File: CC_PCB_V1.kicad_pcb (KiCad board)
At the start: 2 copper layers, 104.2 x 144.9 mm, 8 parts, among them J1 Screw_Terminal_01x07, J2 Antenna_Conn_02x04_Odd_Even, J5 Relay_Conn_01x06, U1 Pico, U2 LM337_TO3

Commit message: Pushing so I can edit on my PC
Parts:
- added J3: USB1130-15-A_REVA, MCU_RaspberryPi_and_Boards:GCT_USB1130-15-A_REVA, F.Cu at (87.0, 150.0)
- moved Screw_Terminal1 120.7 mm to (68.0, 155.0), turned to 180 degrees
- moved U2 116.8 mm to (116.0, 152.0)
- moved C1 113.0 mm to (117.0, 137.0)
- moved C2 106.0 mm to (103.5, 140.0)
- moved J2 35.7 mm to (99.0, 116.0), turned to 180 degrees
- moved J5 26.8 mm to (104.0, 40.0)
- moved U1 8.70 mm to (137.0, 59.5)
- moved J1 2.26 mm to (151.0, 97.0), turned to 270 degrees
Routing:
- net +3.3V: track 167.0 -> 0.00 mm
- net GP6: track 86.0 -> 0.00 mm, vias 2 -> 0
- net GP4: track 78.1 -> 0.00 mm, vias 1 -> 0
- net +5V: track 75.7 -> 0.00 mm
- net GP7: track 74.3 -> 0.00 mm, vias 1 -> 0
- net 3.3V: track 68.5 -> 0.00 mm
- net GP17: track 48.9 -> 0.00 mm
- net GP12: track 45.2 -> 0.00 mm, vias 1 -> 0
- net GP27: track 43.9 -> 0.00 mm
- net GP14: track 43.6 -> 0.00 mm
- net GP22: track 40.5 -> 0.00 mm
- net GP26: track 40.4 -> 0.00 mm
- net GP13: track 40.2 -> 0.00 mm
- net GP21: track 36.8 -> 0.00 mm, vias 1 -> 0
- net GND: track 29.2 -> 0.00 mm, vias 5 -> 0
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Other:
- board text added: "+3.3V"
- board text added: "DIR"
- board text added: "On/Off"
- board text added: "POT1"
- board text added: "POT2"
- board text added: "Step"
- board text added: "Throttle"

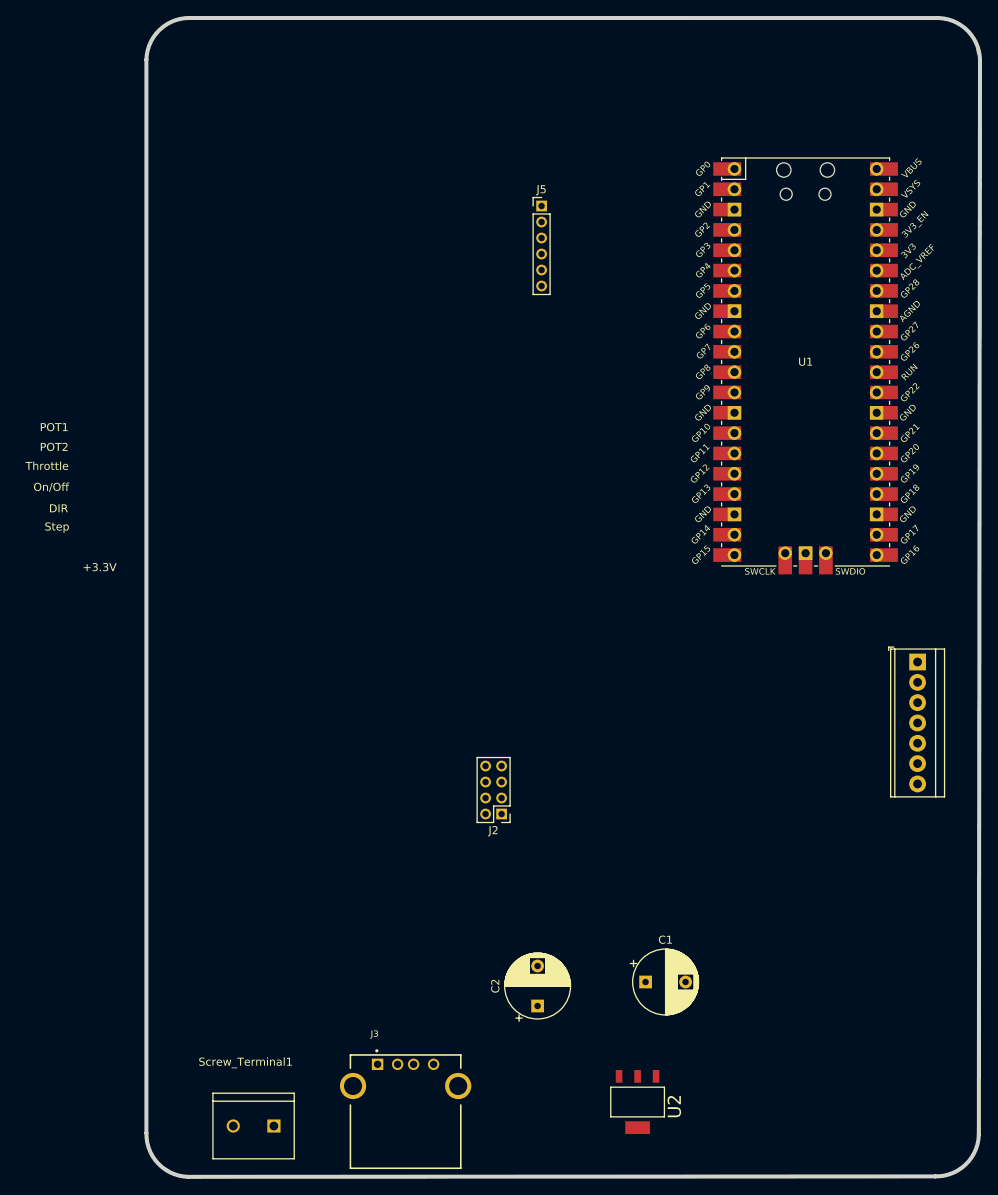
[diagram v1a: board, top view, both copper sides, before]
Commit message: "Finished" PCB
Re did the layout of the board for a better fitment
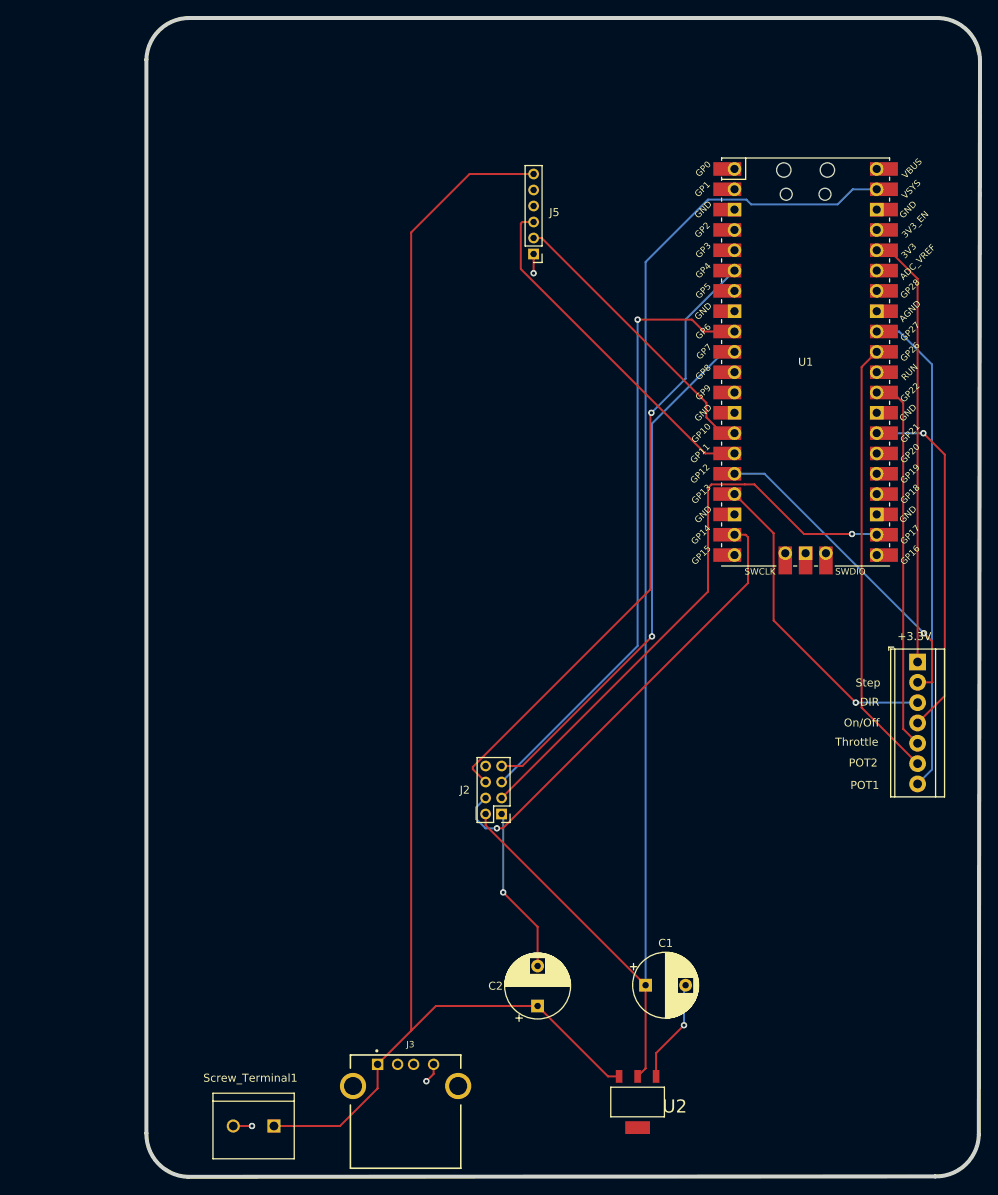
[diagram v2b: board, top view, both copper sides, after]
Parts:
- moved J5 6.08 mm to (103.0, 46.0), turned to 180 degrees
- moved C1 0.40 mm to (117.0, 137.4)
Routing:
- net +5V: track 0.00 -> 172.9 mm
- net +3.3V: track 0.00 -> 165.1 mm
- net GP4: track 0.00 -> 78.1 mm, vias 0 -> 1
- net GP6: track 0.00 -> 77.6 mm, vias 0 -> 1
- net GP17: track 0.00 -> 73.3 mm, vias 0 -> 1
- net GP7: track 0.00 -> 66.1 mm, vias 0 -> 1
- net GP27: track 0.00 -> 61.8 mm
- net GP14: track 0.00 -> 57.8 mm, vias 0 -> 1
- net GP26: track 0.00 -> 55.2 mm
- net 3.3V: track 0.00 -> 54.5 mm
- net GP22: track 0.00 -> 47.1 mm
- net GP21: track 0.00 -> 44.6 mm, vias 0 -> 1
- net GP11: track 0.00 -> 43.6 mm
- net GP12: track 0.00 -> 41.3 mm, vias 0 -> 1
- net GND: track 0.00 -> 41.0 mm, vias 0 -> 5
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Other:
- board text added: "Design by: Jacob Romeo, Daniel Wilczak, Dylan Ballback"
- board text removed: "Design by: Daniel Wilczak, Dylan Ballback, Jacob Romeo"

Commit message: Added 1x2 screw terminal for the POTS
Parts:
- added Screw_Terminal2: 282837-2, MCU_RaspberryPi_and_Boards:TE_282837-2, F.Cu at (150.4, 130.5)
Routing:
- net +3.3V: track 165.1 -> 202.9 mm
- net Net-(J3-PadS1): track 0.00 -> 14.5 mm
- net GND: track 41.0 -> 43.3 mm, vias 5 -> 6
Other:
- board text added: "+5V"
- board text added: "GND"
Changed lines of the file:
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@@
-(kicad_pcb (version 20171130) (host pcbnew "(5.1.9)-1")
+(kicad_pcb (version 20171130) (host pcbnew "(5.1.10)-1")
   (general
     (thickness 1.6)
-    (drawings 25)
-    (tracks 125)
+    (drawings 29)
+    (tracks 135)
     (zones 0)
-    (modules 9)
+    (modules 10)
     (nets 51)
   )
@@
     (add_net "Net-(U1-Pad7)")
     (add_net "Net-(U1-Pad8)")
+  )
+  (module MCU_RaspberryPi_and_Boards:TE_282837-2 (layer F.Cu)
+    (at 150.4 130.5 270)
+    (fp_text reference Screw_Terminal2 (at -6.9 0.3 180) (layer F.SilkS)
+      (effects (font (size 1.002039 1.002039) (thickness 0.15)))
+    )
+    (fp_text value 282837-2 (at 6.7 0 180) (layer F.Fab)
+      (effects (font (size 1.002614 1.002614) (thickness 0.15)))
+    )
+    (fp_line (start -5.08 -4.1) (end 5.08 -4.1) (layer F.SilkS) (width 0.127))
+    (fp_line (start 5.08 -4.1) (end 5.08 3.1) (layer F.SilkS) (width 0.127))
+    (fp_line (start 5.08 3.1) (end 5.08 4.1) (layer F.SilkS) (width 0.127))
+    (fp_line (start 5.08 4.1) (end -5.08 4.1) (layer F.SilkS) (width 0.127))
+    (fp_line (start -5.08 4.1) (end -5.08 3.1) (layer F.SilkS) (width 0.127))
+    (fp_line (start -5.08 3.1) (end -5.08 -4.1) (layer F.SilkS) (width 0.127))
+    (fp_line (start -5.33 -4.35) (end 5.33 -4.35) (layer F.CrtYd) (width 0.05))
+    (fp_line (start 5.33 -4.35) (end 5.33 4.35) (layer F.CrtYd) (width 0.05))
+    (fp_line (start 5.33 4.35) (end -5.33 4.35) (layer F.CrtYd) (width 0.05))
+    (fp_line (start -5.33 4.35) (end -5.33 -4.35) (layer F.CrtYd) (width 0.05))
+    (fp_line (start -5.08 -4.1) (end 5.08 -4.1) (layer F.Fab) (width 0.127))
+    (fp_line (start 5.08 -4.1) (end 5.08 4.1) (layer F.Fab) (width 0.127))
+    (fp_line (start 5.08 4.1) (end -5.08 4.1) (layer F.Fab) (width 0.127))
+    (fp_line (start -5.08 4.1) (end -5.08 -4.1) (layer F.Fab) (width 0.127))
+    (fp_circle (center -2.54 1.27) (end -2.44 1.27) (layer F.Fab) (width 0.2))
+    (fp_line (start -5.08 3.1) (end 5.08 3.1) (layer F.SilkS) (width 0.127))
+    (pad 2 thru_hole circle (at 2.54 0 270) (size 1.65 1.65) (drill 1.1) (layers *.Cu *.Mask)
+      (net 7 GND))
+    (pad 1 thru_hole rect (at -2.54 0 270) (size 1.65 1.65) (drill 1.1) (layers *.Cu *.Mask)
+      (net 42 +3.3V))
   )
   (module MCU_RaspberryPi_and_Boards:GCT_USB1130-15-A_REVA (layer F.Cu)
@@
     )
   )
+  (gr_text GND (at 143.2 133.3) (layer F.SilkS)
+    (effects (font (size 1 1) (thickness 0.15)))
+  )
+  (gr_text +3.3V (at 142.6 128) (layer F.SilkS)
+    (effects (font (size 1 1) (thickness 0.15)))
+  )
+  (gr_text +5V (at 70.4 160.3) (layer F.SilkS)
+    (effects (font (size 1 1) (thickness 0.15)))
+  )
+  (gr_text GND (at 65.4 160.3) (layer F.SilkS)
+    (effects (font (size 1 1) (thickness 0.15)))
+  )
   (gr_line (start 60 121) (end 60 105) (layer Dwgs.User) (width 0.15))
   (gr_line (start 101 121) (end 60 121) (layer Dwgs.User) (width 0.15))
@@
   (via (at 103 48.4) (size 0.8) (drill 0.4) (layers F.Cu B.Cu) (net 7))
   (segment (start 103 46) (end 103 48.4) (width 0.25) (layer F.Cu) (net 7))
+  (via (at 152.5 132.7) (size 0.8) (drill 0.4) (layers F.Cu B.Cu) (net 7))
+  (segment (start 152.16 133.04) (end 152.5 132.7) (width 0.25) (layer F.Cu) (net 7))
+  (segment (start 150.4 133.04) (end 152.16 133.04) (width 0.25) (layer F.Cu) (net 7))
   (segment (start 112.2996 148.7996) (end 103.5 140) (width 0.25) (layer F.Cu) (net 8))
   (segment (start 113.6886 148.7996) (end 112.2996 148.7996) (width 0.25) (layer F.Cu) (net 8))
@@
   (segment (start 142.89 37.91) (end 141 39.8) (width 0.25) (layer B.Cu) (net 42))
   (segment (start 145.89 37.91) (end 142.89 37.91) (width 0.25) (layer B.Cu) (net 42))
+  (segment (start 117 137.4) (end 117.5 137.4) (width 0.25) (layer F.Cu) (net 42))
+  (segment (start 117 137.4) (end 117.2 137.4) (width 0.25) (layer F.Cu) (net 42))
+  (segment (start 126.64 127.96) (end 150.4 127.96) (width 0.25) (layer F.Cu) (net 42))
+  (segment (start 117.2 137.4) (end 126.64 127.96) (width 0.25) (layer F.Cu) (net 42))
   (segment (start 103 42) (end 101.6 42) (width 0.25) (layer F.Cu) (net 44))
   (segment (start 101.6 42) (end 101.4 42.2) (width 0.25) (layer F.Cu) (net 44))
@@
   (segment (start 126.564998 68.39) (end 128.11 68.39) (width 0.25) (layer F.Cu) (net 45))
   (segment (start 104 44) (end 124.6 64.6) (width 0.25) (layer F.Cu) (net 45))
+  (segment (start 91.932001 151.637999) (end 93.57 150) (width 0.25) (layer B.Cu) (net 48))
+  (segment (start 82.067999 151.637999) (end 91.932001 151.637999) (width 0.25) (layer B.Cu) (net 48))
+  (segment (start 80.43 150) (end 82.067999 151.637999) (width 0.25) (layer B.Cu) (net 48))
   (zone (net 7) (net_name GND) (layer F.Cu) (hatch edge 0.508)
     (connect_pads (clearance 0.508))

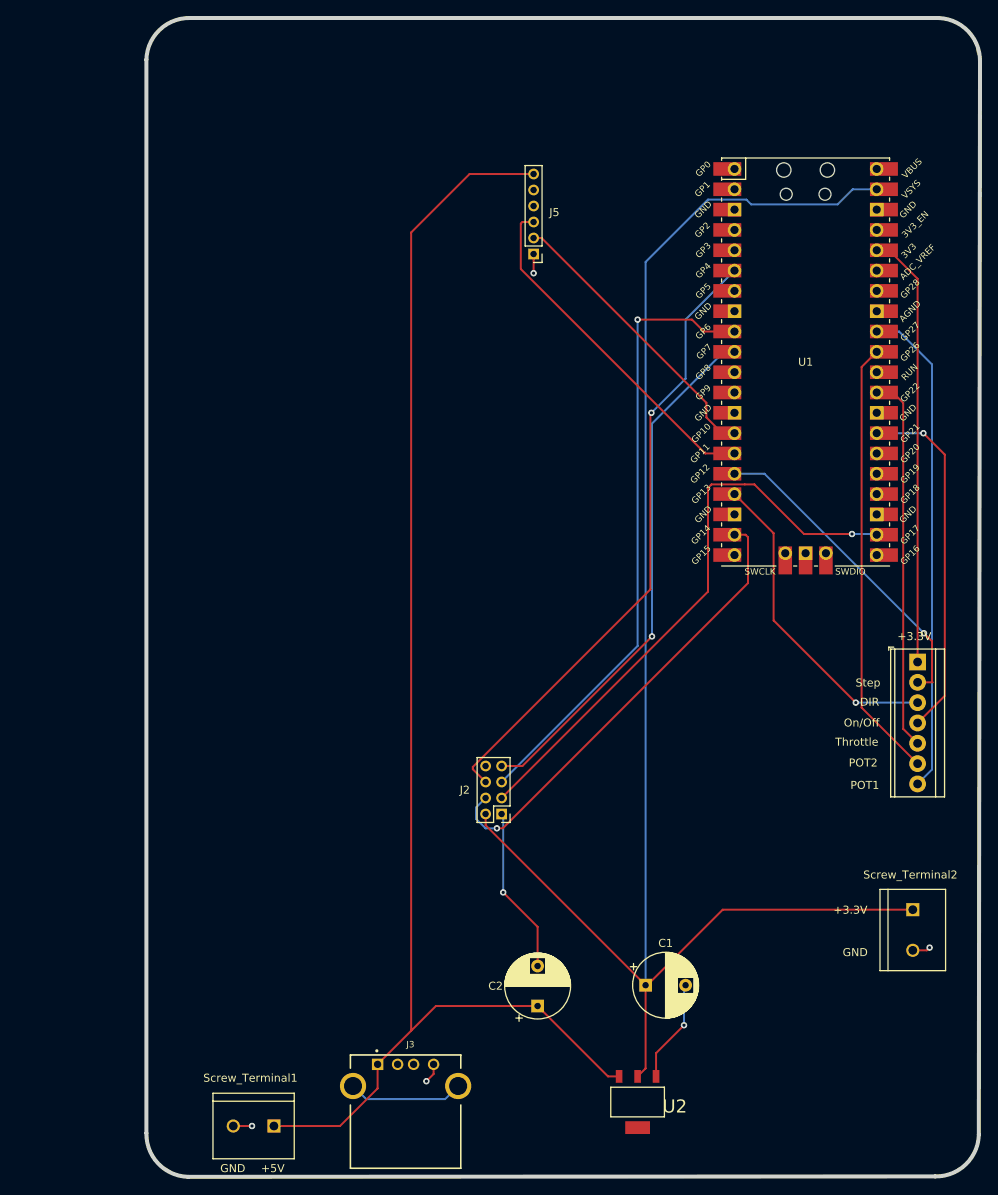
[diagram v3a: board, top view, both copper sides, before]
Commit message: Added mounting holes
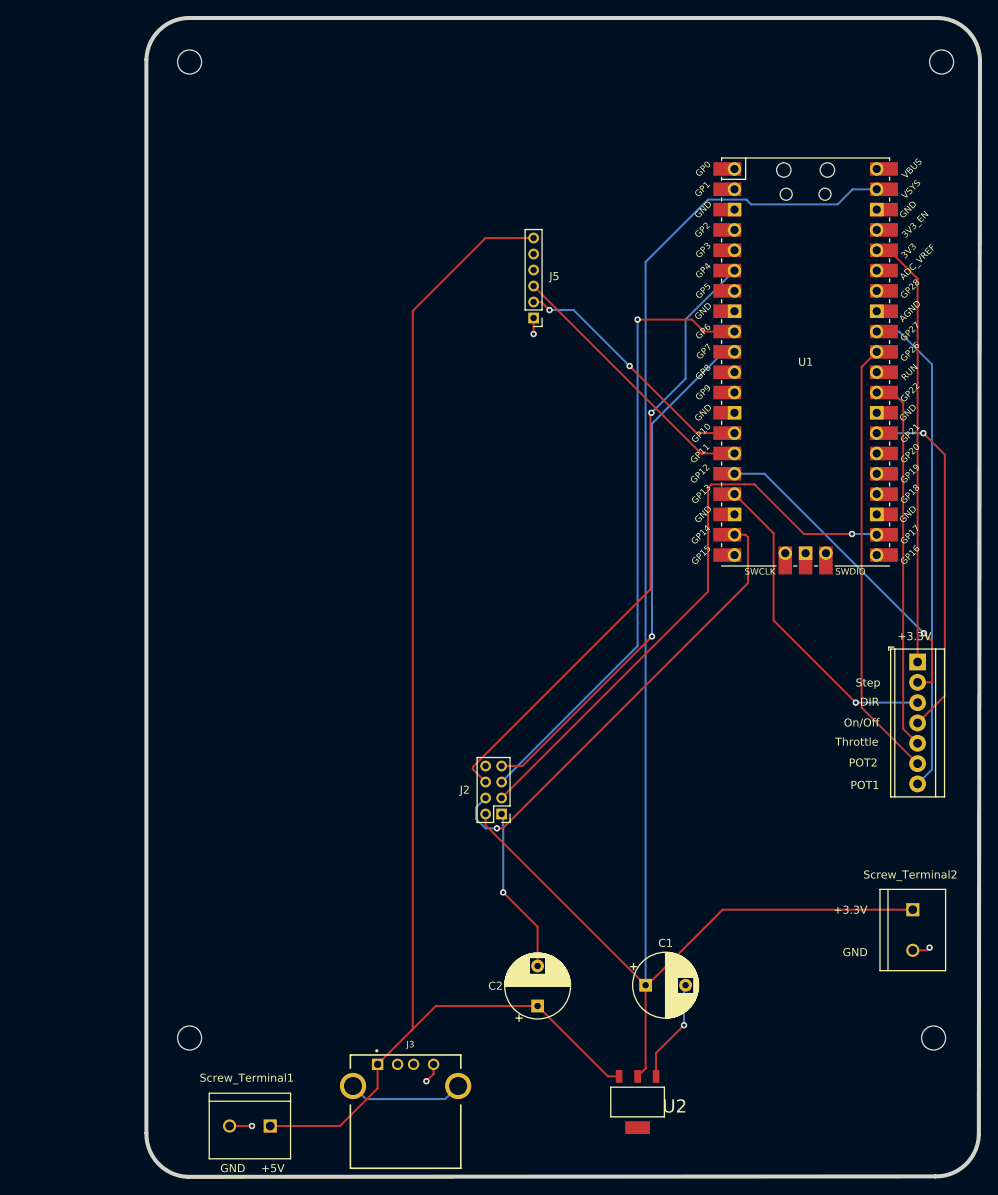
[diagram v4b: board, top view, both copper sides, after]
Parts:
- added H1: MountingHole, MountingHole:MountingHole_3mm, F.Cu at (154.0, 22.0)
- added H2: MountingHole, MountingHole:MountingHole_3mm, F.Cu at (60.0, 144.0)
- added H3: MountingHole, MountingHole:MountingHole_3mm, F.Cu at (60.0, 22.0)
- added H4: MountingHole, MountingHole:MountingHole_3mm, F.Cu at (153.0, 144.0)
- moved J5 8.00 mm to (103.0, 54.0)
- moved Screw_Terminal1 0.46 mm to (67.5, 155.0)
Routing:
- net GP11: track 43.6 -> 33.8 mm
- net +5V: track 172.9 -> 163.4 mm
- net GP10: track 36.3 -> 31.9 mm, vias 0 -> 2
